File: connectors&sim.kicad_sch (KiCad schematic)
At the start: 29 parts, among them J1 43650-0516, J2 43650-0516, J3 43650-0216, J4 43650-0416, J5 43045-1013, J6 43650-0616, J7 43650-0216

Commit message: add some silkscreens
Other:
- note added: "To IMD IMD+ IMD-"
- note removed: "To IMD HV+ HV-"
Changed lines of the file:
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@@
 		)
 	)
-	(text "To IMD\n\nHV+\n\n\n\nHV-"
+	(text "To IMD\n\nIMD+\n\n\n\nIMD-"
 		(exclude_from_sim no)
 		(at 80.772 163.068 0)

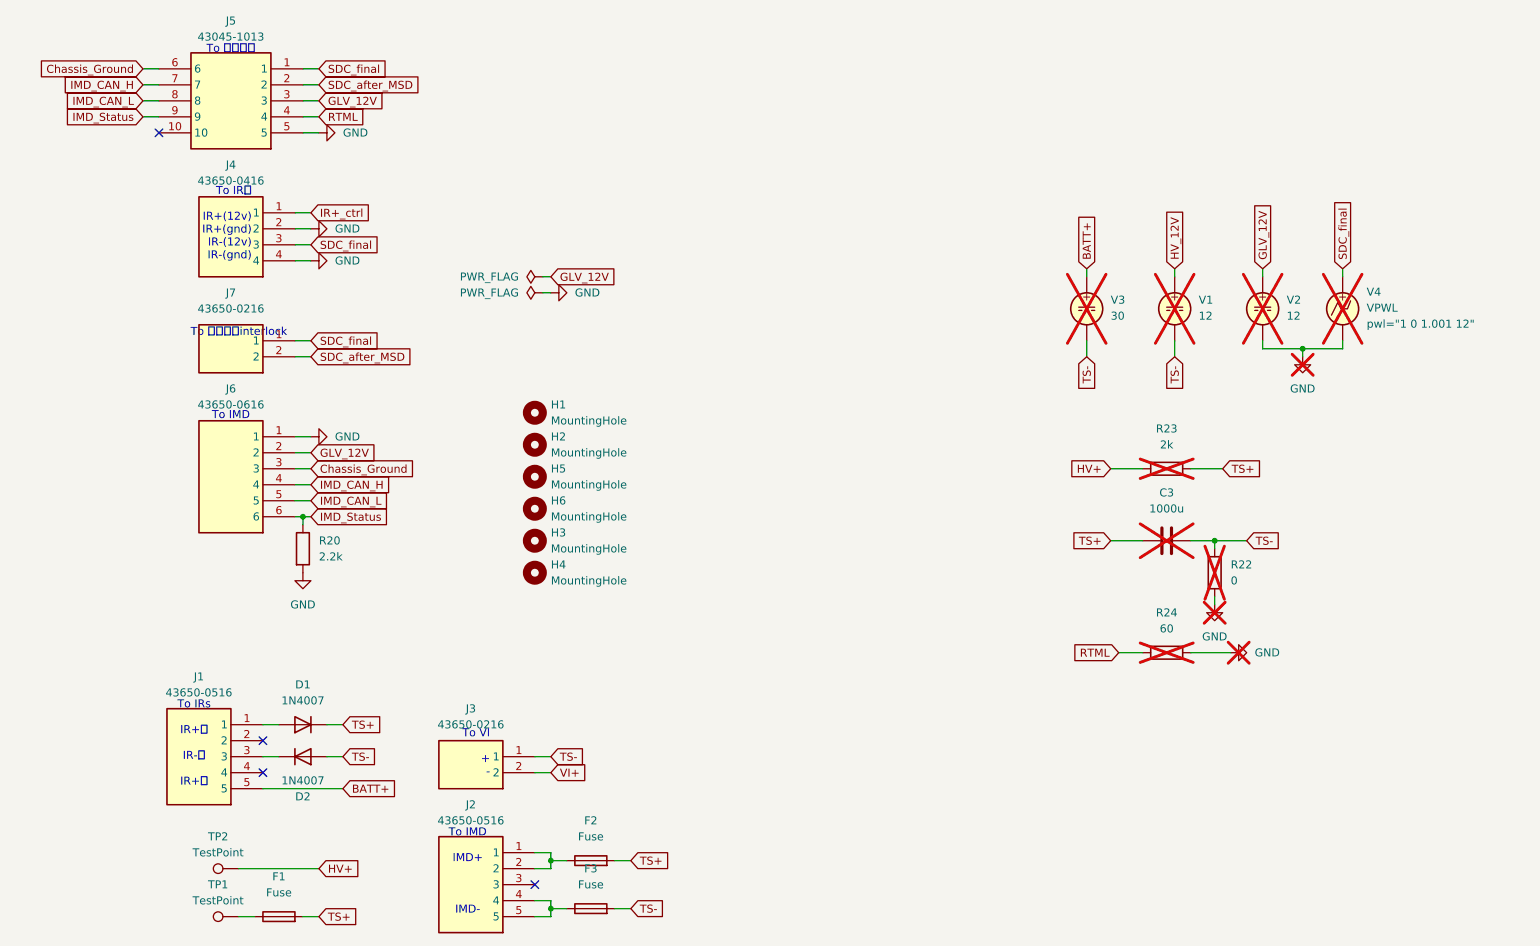
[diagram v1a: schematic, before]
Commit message: add mouser part numbers
change resisters footprints of 0805 to 1206 for 500V voltage rating
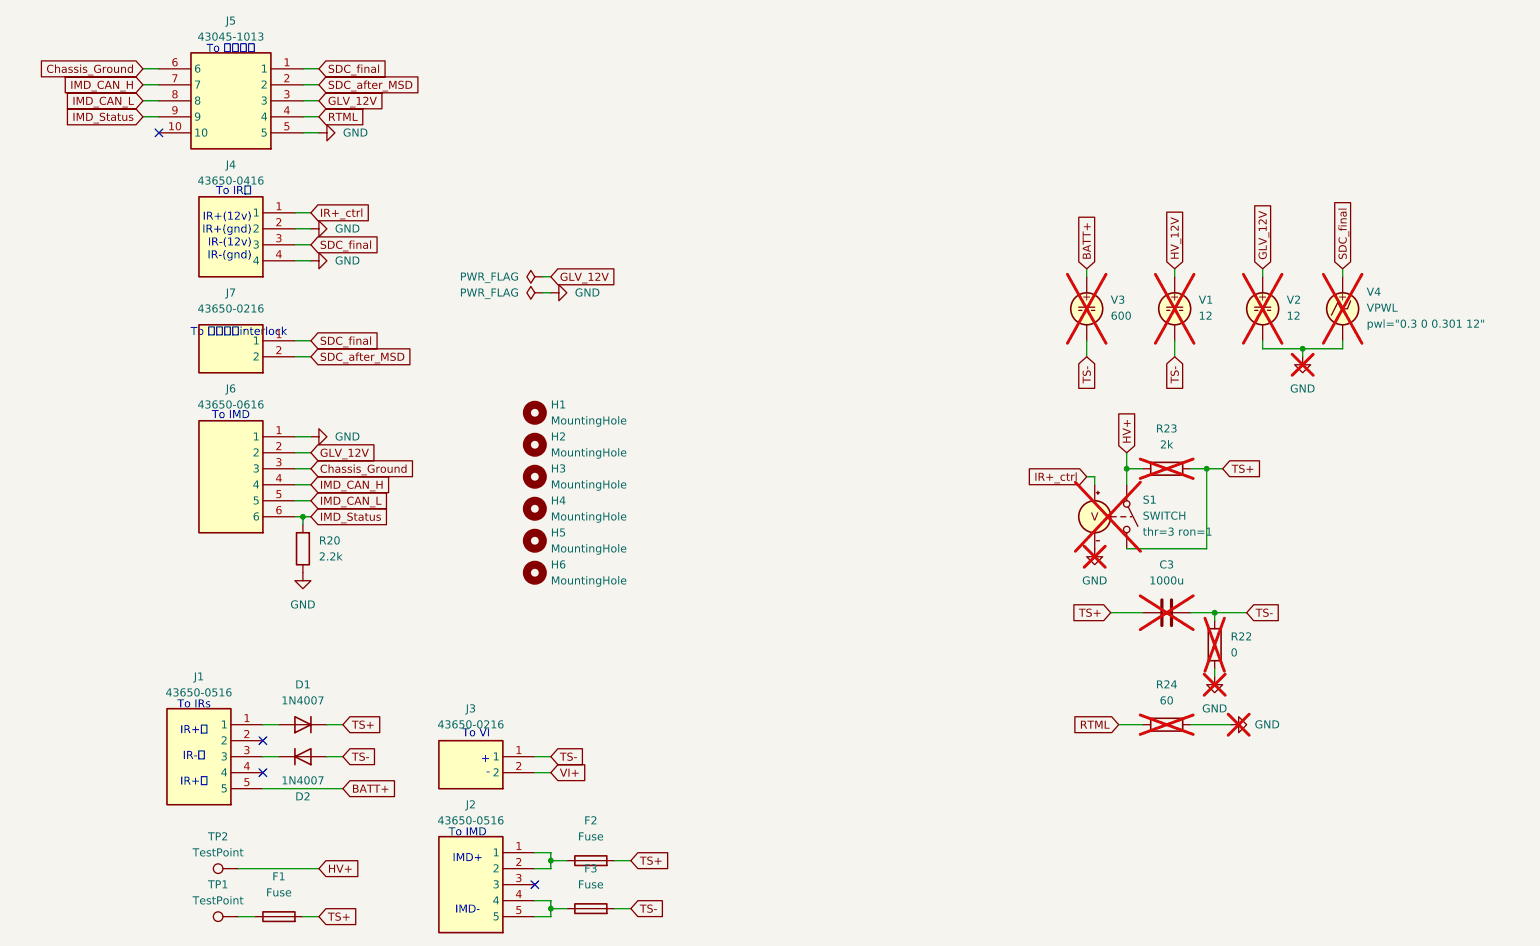
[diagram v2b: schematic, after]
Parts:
- added S1: SWITCH, symbol Simulation_SPICE:SWITCH
- D1, D2: Mouser Part Number (none) -> 637-1N4007
- F1, F2, F3: Manufacturer_Part_Number (none) -> 0ADKP1000-RE; Mouser Part Number (none) -> 530-0ADKP1000-RE
- R20: footprint Resistor_SMD:R_0805_2012Metric_Pad1.20x1.40mm_HandSolder -> Resistor_SMD:R_1206_3216Metric_Pad1.30x1.75mm_HandSolder; Mouser Part Number (none) -> 667-ERJ-P08J222V
- V3: value 30 -> 600
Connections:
- net GND: now also R20.1, S1.4 (C-); no longer R20.2
- net HV+: now also S1.1 (N+)
- net IMD_Status: now also R20.2; no longer R20.1
- net IR+_ctrl: now also S1.3 (C+)
- net TS+: now also S1.2 (N-)
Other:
- moved on the sheet: C3, H3, H4, H5, H6, R20, R22, R24
